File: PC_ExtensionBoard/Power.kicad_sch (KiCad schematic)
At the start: 1 part

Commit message: update schematic: add pattern
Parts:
- added C204, C205, C48, C53, C54, C55: C_100n_0402, antmicro-footprints:C_0402_1005Metric, symbol antmicroCapacitors0402:C_100n_0402
- added C39: C_Pol_68u_16V_Panasonic-TQC-D, antmicro-footprints:C_Pol_EIA-D, symbol antmicroCapacitorspol:C_Pol_68u_16V_Panasonic-TQC-D
- added C40, C58, C59: C_22u_16V_0603, antmicro-footprints:C_0603_1608Metric, symbol antmicroCapacitors0603:C_22u_16V_0603
- added C45, C50, C57, C62, C66, C67, C69, C70: C_1u_0402, antmicro-footprints:C_0402_1005Metric, symbol antmicroCapacitors0402:C_1u_0402
- added C52, C64: C_Pol_100u_10V_KEMET-T520-B, antmicro-footprints:C_Pol_EIA-B, symbol antmicroCapacitorspol:C_Pol_100u_10V_KEMET-T520-B
- added C61: 1uF/16V, A_HDJ_Library:C_0402_1005Metric, symbol Device:C
- added D10, D11, D14, D19: 0402ESDA-05N, A_HDJ_Library:D_0402_1005Metric, symbol Diode:ESD9B5.0ST5G
- added D12: PESD24VS1UL-N, A_HDJ_Library:D_0402_1005Metric, symbol Device:D_Zener
- added D36: BAT54C, antmicro-footprints:SOT-23-3, symbol antmicroDiodesRectifiersSingle:BAT54C
- added D6: TPD2E2U06_SC70, antmicro-footprints:SC70-3, symbol antmicroTVSDiodes:TPD2E2U06_SC70
- added J18: USB_C_Receptacle_USB2.0, A_HDJ_Library:USB_C_Receptacle_G-Switch_GT-USB-7010ASV, symbol Connector:USB_C_Receptacle_USB2.0
- added L2: L_1u8_14A_Coilcraft-XAL6030, antmicro-footprints:L_Coilcraft-XAL6030, symbol antmicroFixedInductors:L_1u8_14A_Coilcraft-XAL6030
- added L3: L_1u8_6.8A_WE-MAPI-4020, antmicro-footprints:L_WE-MAPI-4020, symbol antmicroFixedInductors:L_1u8_6.8A_WE-MAPI-4020
- added Q3: BSS138-7-F, antmicro-footprints:SOT-23-3, symbol antmicroTransistorsFETsMOSFETsSingle:BSS138-7-F
- added Q4: SI7613DN-T1-GE3, antmicro-footprints:Vishay_PowerPAK_1212-8_Single, symbol antmicroTransistorsFETsMOSFETsSingle:SI7613DN-T1-GE3
- added R100, R107, R110: R_15k_0402, antmicro-footprints:R_0402_1005Metric, symbol antmicroResistors0402:R_15k_0402
- added R101, R118: R_100k_0402, antmicro-footprints:R_0402_1005Metric, symbol antmicroResistors0402:R_100k_0402
- added R102, R115, R119: R_0R_0402, antmicro-footprints:R_0402_1005Metric, symbol antmicroResistors0402:R_0R_0402
- added R104, R113: R_0R001_0805, antmicro-footprints:R_0805_2012Metric, symbol antmicroResistorsmisc:R_0R001_0805
- added R105: R_1k_0402, antmicro-footprints:R_0402_1005Metric, symbol antmicroResistors0402:R_1k_0402
- added R108, R116, R86, R92, R96: R_10k_0402, antmicro-footprints:R_0402_1005Metric, symbol antmicroResistors0402:R_10k_0402
- added R109: R_110k_0402, antmicro-footprints:R_0402_1005Metric, symbol antmicroResistors0402:R_110k_0402
- added R117, R87: R_30k_0402, antmicro-footprints:R_0402_1005Metric, symbol antmicroResistors0402:R_30k_0402
- added R37: 10K/1%, A_DFRobot:R_0402, symbol Device:R
- added R40: 1K/1%, A_DFRobot:R_0402, symbol Device:R
- added R47: 56K/1%, A_DFRobot:R_0402, symbol Device:R
- added R91, R99: R_68k_0402, antmicro-footprints:R_0402_1005Metric, symbol antmicroResistors0402:R_68k_0402
- added U19: TPS56C230, antmicro-footprints:QFN-20-1EP_3x3mm_P0.45mm_TPS56xxxx, symbol antmicroDCDCConverters:TPS56C230
- added U20: TPS3840PL30DBVR, antmicro-footprints:SOT-23-5, symbol antmicroPMICPowerSequencers:TPS3840PL30DBVR
- added U21: TPS564247DRLR, antmicro-footprints:SOT-563, symbol antmicroDCDCConverters:TPS564247DRLR
- added U23: TLV73333PDBVT, antmicro-footprints:SOT-23-5, symbol antmicroPMICVoltageRegulatorsLinear:TLV73333PDBVT
- added U49, U50: INA219AIDCNR, antmicro-footprints:SOT-23-8, symbol antmicroPowerMeasurement:INA219AIDCNR
- added U9: CH224K, A_HDJ_Library:ESSOP-10-1EP_3.9x5mm_P1.0mm_EP3.2x2.3, symbol USB PD & DC Input-altium-import:root_0_CH224K
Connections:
- new net: Q3.1 (G), R115.2, R116.1, R117.1
- new net: C61.1, R40.2, U9.1 (VDD)
- new net: C45.2, R91.2, R96.2, U19.17 (V_{CC})
- new net: R107.1, R108.2, U21.5 (EN)
- new net: D36.1, D36.2, R86.1, R87.1, U19.12 (EN)
- new net: C69.2, R119.1, U23.5 (VOUT)
- new net: R102.2, U20.4 (~{MR})
- new net: C53.2, C55.2, U20.5 (CT)
- new net: C48.1, U19.1 (BST)
- new net: R100.2, R99.1, U19.14 (FB)
- new net: R91.1, R92.2, U19.15 (MODE)
- new net: C48.2, L2.1, U19.19 (SW), U19.20 (SW), U19.6 (SW)
- new net: R109.1, R110.2, U21.6 (FB)
- new net: C62.2, C64.1, L3.2, R109.2, R113.1, U50.1 (IN+)
- new net: C50.2, C52.1, L2.2, R104.1, R99.2, U49.1 (IN+)
- new net: Q3.3 (D), Q4.4 (G), R118.1
- new net: R37.2, U9.8 (VBUS)
- new net: R47.1, U9.9 (CFG1)
- new net: L3.1, U21.2 (SW)
- new net +12V: R116.2
- new net +12V_AON: C39.1, C40.2, C58.2, C59.2, R107.2, U19.2 (V_{IN}), U19.3 (V_{IN}), U19.4 (V_{IN}), U19.5 (V_{IN}), U21.1 (V_{IN})
- new net +15V: D12.1 (K), J18.A4 (VBUS), J18.A9 (VBUS), J18.B4 (VBUS), J18.B9 (VBUS), R37.1, R40.1
- new net +3V3: C57.2, R104.2, U49.2 (IN-)
- new net +3V3_AON: C204.2, C205.2, C54.2, R119.2, U20.2 (VDD), U49.4 (V_{S}), U49.7 (A0), U50.4 (V_{S})
- new net +5V: C70.2, Q4.5 (D), R86.2
- new net +5V_AON: C66.2, C67.2, Q4.1 (S), Q4.2 (S), Q4.3 (S), R113.2, R118.2, U23.1 (VIN), U23.3 (EN), U50.2 (IN-)
- new net CC1: D14.2 (A2), J18.A5 (CC1), U9.7 (CC1)
- new net CC2: D19.2 (A2), J18.B5 (CC2), U9.6 (CC2)
- new net GND: C204.1, C205.1, C39.2, C40.1, C45.1, C50.1, C52.2, C53.1, C54.1, C55.1, C57.1, C58.1, C59.1, C61.2, C62.1, C64.2, C66.1, C67.1, C69.1, C70.1, D10.1 (A1), D11.1 (A1), D12.2 (A), D14.1 (A1), D19.1 (A1), D6.3, J18.A1 (GND), J18.A12 (GND), J18.B1 (GND), J18.B12 (GND), J18.S1 (SHIELD), Q3.2 (S), R100.1, R101.1, R105.1, R108.1, R110.1, R117.2, R47.2, R87.2, R92.1, U19.13 (AGND), U19.18 (PGND), U19.21 (PGND), U19.7 (PGND), U19.8 (PGND), U20.3 (GND), U21.3 (GND), U21.4 (AGND), U23.2 (GND), U49.3 (GND), U49.8 (A1), U50.3 (GND), U50.8 (A1), U9.0 (GND)
- new net I2C.SCL: U49.5 (SCL), U50.5 (SCL)
- new net I2C.SDA: U49.6 (SDA), U50.6 (SDA), U50.7 (A0)
- new net PG_{1V0}: R101.2, R102.1
- new net PG_{3V3}: R96.1, U19.9 (PG)
- new net PSON: D36.3
- new net PWRBTN: D6.2
- new net PWR_C_D+: D11.2 (A2), J18.A6 (D+), J18.B6 (D+), U9.4 (DP)
- new net PWR_C_D-: D10.2 (A2), J18.A7 (D-), J18.B7 (D-), U9.5 (DM)
- new net PWR_OK: R105.2, U20.1 (~{RESET})
- new net ~{RESET}: R115.1
- no-connect marks 0 -> 7
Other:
- note added: "+3V3 DC/DC converter"
- note added: "+3V3_AON LDO"
- note added: "+5V DC/DC converter"
- note added: "15V PD Input"
- note added: "1V0 is last in PG chain so then if it's PG is high all rails should be OK"
- note added: "ADDR: 0x41"
- note added: "ADDR: 0x42"
- note added: "CH224K get DC 15V power from USB-PD adapter"
- note added: "PSU rail description: * +12V_{AON} - Input power Always on rails: * +5V_{AON} * +3V3_{AON} Board rails (PSON == 1): * +12V * +5V * +3V3 * +1V8 * +1V0"
- note added: "Sequence: +5V_{AON} +3V3_{AON} *Power button* +12V +5V +3V3 +1V8 +1V0"
- note added: "V_{out} = 3.3 V f_{SW} = 500 kHz I_{L} = 11.0 A ΔI_{L} = 25% I_{Lpeak} = 12.4 A"
- note added: "V_{out} = 5.0 V f_{SW} = 1200 kHz I_{L} = 4.0 A ΔI_{L} = 34% I_{Lpeak} = 4.68 A"
- note added: "~120 ms delay"

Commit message: components placement R1
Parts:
- C61: footprint A_HDJ_Library:C_0402_1005Metric -> PC_Components_1:C_0402_1005Metric; DF_Comment 贴片电容0402-1uF-16V-X5R(0402) -> (none); SCH_Show_Footprint C0402 -> (none)
- D10, D11, D14, D19: footprint A_HDJ_Library:D_0402_1005Metric -> PC_Components_1:C_0402_1005Metric; DF_Comment 5.0V双向静电保护管_0402ESDA-05N -> (none); LCSC (none) -> C316049; SCH_Show_Footprint D0402 -> (none)
- D12: footprint A_HDJ_Library:D_0402_1005Metric -> PC_Components_1:C_0402_1005Metric; Buy_Link https://item.szlcsc.com/393990.html -> (none); DF_Comment 单向静电保护二极管_PESD24VS1UL-N_DFN1006 -> (none); LCSC (none) -> C406227
- R37: footprint A_DFRobot:R_0402 -> PC_Components_1:R_0402_1005Metric; DF_Comment 贴片电阻0402-10K-1% -> (none)
- R40: footprint A_DFRobot:R_0402 -> PC_Components_1:R_0402_1005Metric; DF_Comment 贴片电阻0402-1K-1% -> (none)
- R47: value 56K/1% -> 24K/1%; footprint A_DFRobot:R_0402 -> PC_Components_1:C_0402_1005Metric; DF_Comment 贴片电阻0402-56K-1%(0402) -> (none)
- U9: footprint A_HDJ_Library:ESSOP-10-1EP_3.9x5mm_P1.0mm_EP3.2x2.3 -> PC_ExtensionBoard:ESSOP-10_L4.9-W3.9-P1.0-LS6.0-TL-EP; DF_Comment USB PD等快充协议受电芯片-CH224K-ESSOP10 -> (none); LCSC (none) -> C970725
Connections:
- net +15V is gone; now on net +12V: D12.1 (K), J18.A4 (VBUS), J18.A9 (VBUS), J18.B4 (VBUS), J18.B9 (VBUS), R37.1, R40.1
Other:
- note added: "12V PD Input"
- note added: "CH224K get DC 12V power from USB-PD adapter"
- note removed: "15V PD Input"
- note removed: "1V0 is last in PG chain so then if it's PG is high all rails should be OK"
- note removed: "CH224K get DC 15V power from USB-PD adapter"
- note removed: "PSU rail description: * +12V_{AON} - Input power Always on rails: * +5V_{AON} * +3V3_{AON} Board rails (PSON == 1): * +12V * +5V * +3V3 * +1V8 * +1V0"
- note removed: "Sequence: +5V_{AON} +3V3_{AON} *Power button* +12V +5V +3V3 +1V8 +1V0"
- moved on the sheet: C53, C54, C55, C61, D10, D11, D12, D14, D19, J18, R101, R102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

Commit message: refactor project
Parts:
- C204, C205, C48, C53, C54, C55: symbol antmicroCapacitors0402:C_100n_0402 -> A_PC_ExtensionBoard:C_100n_0402
- C39: symbol antmicroCapacitorspol:C_Pol_68u_16V_Panasonic-TQC-D -> A_PC_ExtensionBoard:C_Pol_68u_16V_Panasonic-TQC-D
- C40, C58, C59: symbol antmicroCapacitors0603:C_22u_16V_0603 -> A_PC_ExtensionBoard:C_22u_16V_0603
- C45, C50, C57, C62, C66, C67, C69, C70: symbol antmicroCapacitors0402:C_1u_0402 -> A_PC_ExtensionBoard:C_1u_0402
- C52, C64: symbol antmicroCapacitorspol:C_Pol_100u_10V_KEMET-T520-B -> A_PC_ExtensionBoard:C_Pol_100u_10V_KEMET-T520-B
- D36: symbol antmicroDiodesRectifiersSingle:BAT54C -> A_PC_ExtensionBoard:BAT54C
- D6: footprint antmicro-footprints:SC70-3 -> PC_Components_1:SC70-3; symbol antmicroTVSDiodes:TPD2E2U06_SC70 -> A_PC_ExtensionBoard:TPD2E2U06_SC70; LCSC (none) -> C1855726
- DC1: symbol ACLAB_Symbol:root_0_DC-044A-20A_ -> A_PC_ExtensionBoard:DC-044A-20A_
- L2: symbol antmicroFixedInductors:L_1u8_14A_Coilcraft-XAL6030 -> A_PC_ExtensionBoard:L_1u8_14A_Coilcraft-XAL6030
- L3: symbol antmicroFixedInductors:L_1u8_6.8A_WE-MAPI-4020 -> A_PC_ExtensionBoard:L_1u8_6.8A_WE-MAPI-4020
- Q3: symbol antmicroTransistorsFETsMOSFETsSingle:BSS138-7-F -> A_PC_ExtensionBoard:BSS138-7-F
- Q4: symbol antmicroTransistorsFETsMOSFETsSingle:SI7613DN-T1-GE3 -> A_PC_ExtensionBoard:SI7613DN-T1-GE3
- R100, R107, R110: symbol antmicroResistors0402:R_15k_0402 -> A_PC_ExtensionBoard:R_15k_0402
- R101, R118: symbol antmicroResistors0402:R_100k_0402 -> A_PC_ExtensionBoard:R_100k_0402
- R102, R115, R119: symbol antmicroResistors0402:R_0R_0402 -> A_PC_ExtensionBoard:R_0R_0402
- R104, R113: symbol antmicroResistorsmisc:R_0R001_0805 -> A_PC_ExtensionBoard:R_0R001_0805
- R105: symbol antmicroResistors0402:R_1k_0402 -> A_PC_ExtensionBoard:R_1k_0402
- R108, R116, R86, R92, R96: symbol antmicroResistors0402:R_10k_0402 -> A_PC_ExtensionBoard:R_10k_0402
- R109: symbol antmicroResistors0402:R_110k_0402 -> A_PC_ExtensionBoard:R_110k_0402
- R117, R87: symbol antmicroResistors0402:R_30k_0402 -> A_PC_ExtensionBoard:R_30k_0402
- R91, R99: symbol antmicroResistors0402:R_68k_0402 -> A_PC_ExtensionBoard:R_68k_0402
- U19: symbol antmicroDCDCConverters:TPS56C230 -> A_PC_ExtensionBoard:TPS56C230
- U20: symbol antmicroPMICPowerSequencers:TPS3840PL30DBVR -> A_PC_ExtensionBoard:TPS3840PL30DBVR
- U21: symbol antmicroDCDCConverters:TPS564247DRLR -> A_PC_ExtensionBoard:TPS564247DRLR
- U23: symbol antmicroPMICVoltageRegulatorsLinear:TLV73333PDBVT -> A_PC_ExtensionBoard:TLV73333PDBVT
- U49, U50: symbol antmicroPowerMeasurement:INA219AIDCNR -> A_PC_ExtensionBoard:INA219AIDCNR
- U9: symbol USB PD & DC Input-altium-import:root_0_CH224K -> A_PC_ExtensionBoard:CH224K
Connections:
- net +3V3 renamed +3.3V

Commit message: re-link symbol
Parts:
- added BT1: Battery CMOS, Connector_JST:JST_PH_B2B-PH-K_1x02_P2.00mm_Vertical, symbol Device:Battery
- added D5: D_Schottky, symbol Device:D_Schottky
- added R15: R_470R_0402, PC_Components_1:R_0402_1005Metric, symbol A_PC_ExtensionBoard:R_470R_0402
- added SW1: K2-1808SN-A4SW, PC_Components_1:KEY-SMD_4P-L4.2-W3.2-P2.20-LS5.1-TL, symbol A_PC_ExtensionBoard:K2-1808SN-A4SW
- C204, C205, C53, C54, C55, C57, C66, C67, C69, C70: footprint antmicro-footprints:C_0402_1005Metric -> PC_Components_1:C_0402_1005Metric
- D36, Q3: footprint antmicro-footprints:SOT-23-3 -> PC_Components_1:SOT-23-3
- L2: footprint antmicro-footprints:L_Coilcraft-XAL6030 -> PC_Components_1:L_Coilcraft-XAL6030
- L3: footprint antmicro-footprints:L_WE-MAPI-4020 -> PC_Components_1:L_WE-MAPI-4020
- Q4: footprint antmicro-footprints:Vishay_PowerPAK_1212-8_Single -> PC_Components_1:Vishay_PowerPAK_1212-8_Single
- R100, R101, R102, R105, R107, R108, R109, R110, R115, R116, R117, R118, R119, R86, R87, R91, R92, R96, R99: footprint antmicro-footprints:R_0402_1005Metric -> PC_Components_1:R_0402_1005Metric
- R104, R113: footprint antmicro-footprints:R_0805_2012Metric -> PC_Components_1:R_0402_1005Metric
- U19: footprint antmicro-footprints:QFN-20-1EP_3x3mm_P0.45mm_TPS56xxxx -> PC_Components_1:QFN-20-1EP_3x3mm_P0.45mm_TPS56xxxx
- U20, U23: footprint antmicro-footprints:SOT-23-5 -> PC_Components_1:SOT-23-5
- U21: footprint antmicro-footprints:SOT-563 -> PC_Components_1:SOT-563
- U49, U50: footprint antmicro-footprints:SOT-23-8 -> PC_Components_1:SOT-23-8
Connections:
- net GND: now also BT1.2 (-), SW1.1, SW1.2
- net PWRBTN: now also SW1.3, SW1.4
- new net: BT1.1 (+), R15.1
- new net: D5.2 (A), R15.2
- new net VCC_RTC: D5.1 (K)

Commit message: update LCSC for HDMI
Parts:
- removed J18: USB_C_Receptacle_USB2.0, A_HDJ_Library:USB_C_Receptacle_G-Switch_GT-USB-7010ASV, symbol Connector:USB_C_Receptacle_USB2.0
- added USBC1: J18, PC_Components_1:USB-C_SMD-TYPE-C-31-M-12_1, symbol A_PC_ExtensionBoard:root_0_TYPE-C-31-M-12__1
- C204, C205, C48, C53, C54, C55: LCSC (none) -> C85960
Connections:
- net +12V: now also USBC1.A4B9 (VBUS), USBC1.B4A9 (VBUS)
- net CC1: now also USBC1.A5 (CC1)
- net CC2: now also USBC1.B5 (CC2)
- net GND: now also USBC1.1 (EH), USBC1.2 (EH), USBC1.3 (EH), USBC1.4 (EH), USBC1.A1B12 (GND), USBC1.B1A12 (GND)
- net PWR_C_D+: now also USBC1.A6 (DP1), USBC1.B6 (DP2)
- net PWR_C_D-: now also USBC1.A7 (DN1), USBC1.B7 (DN2)
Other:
- moved on the sheet: D6, DC1, SW1

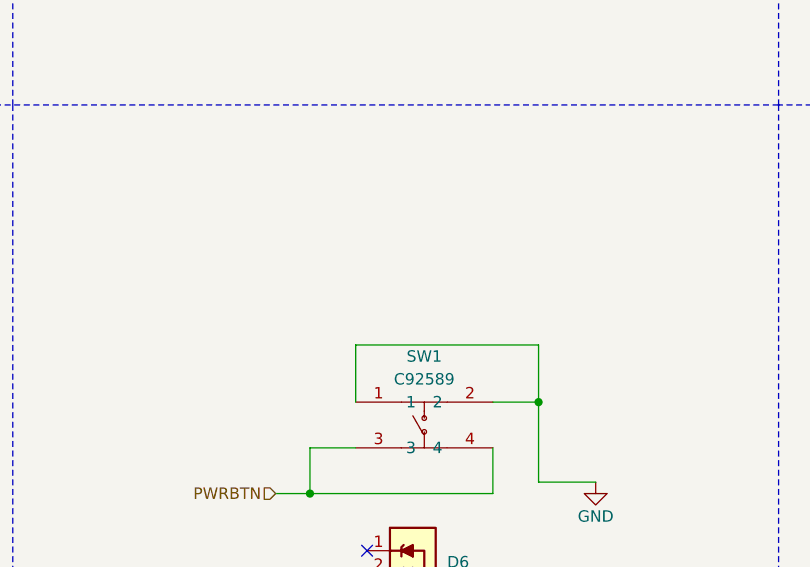
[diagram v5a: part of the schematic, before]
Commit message: update LCSC
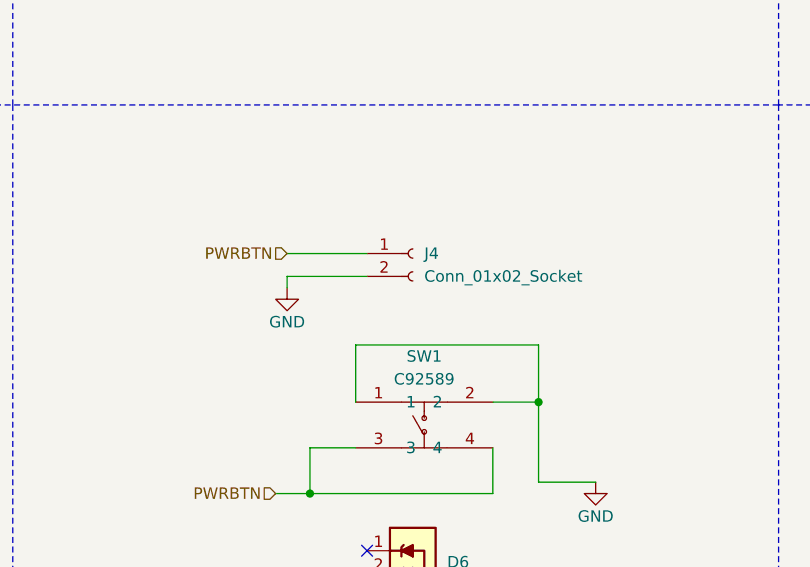
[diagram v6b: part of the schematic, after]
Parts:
- added J4: Conn_01x02_Socket, PC_Components_1:CONN-SMD_2P-P2.00_BX-PH2.0-2PWT, symbol Connector:Conn_01x02_Socket
- D5: footprint (none) -> PC_Components_1:D_SOD-323; LCSC (none) -> C168799
- R15: LCSC (none) -> C2077077
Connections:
- net GND: now also J4.2 (Pin_2)
- net PWRBTN: now also J4.1 (Pin_1)

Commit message: schematic changes
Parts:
- added D8: TPD2E2U06_SC70, PC_Components_1:SC70-3, symbol A_PC_ExtensionBoard:TPD2E2U06_SC70
- added J5: Conn_01x02_Socket, PC_Components_1:CONN-SMD_2P-P2.00_BX-PH2.0-2PWT, symbol Connector:Conn_01x02_Socket
- added SW2: K2-1808SN-A4SW, PC_Components_1:KEY-SMD_4P-L4.2-W3.2-P2.20-LS5.1-TL, symbol A_PC_ExtensionBoard:K2-1808SN-A4SW
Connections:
- net GND: now also D8.3, J5.2 (Pin_2), SW2.1, SW2.2
- new net RESETBTN: D8.2, J5.1 (Pin_1), SW2.3, SW2.4
- no-connect marks 7 -> 8
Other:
- moved on the sheet: C66, C69, R119, U23

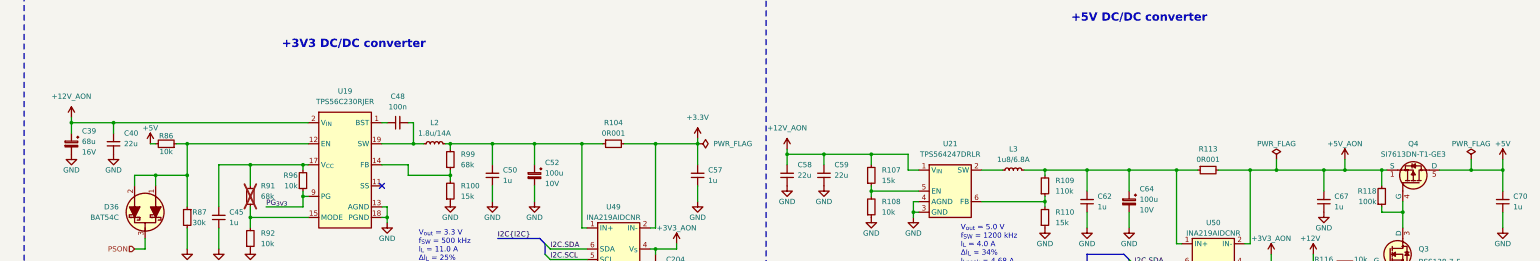
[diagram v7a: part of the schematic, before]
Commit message: update schematic
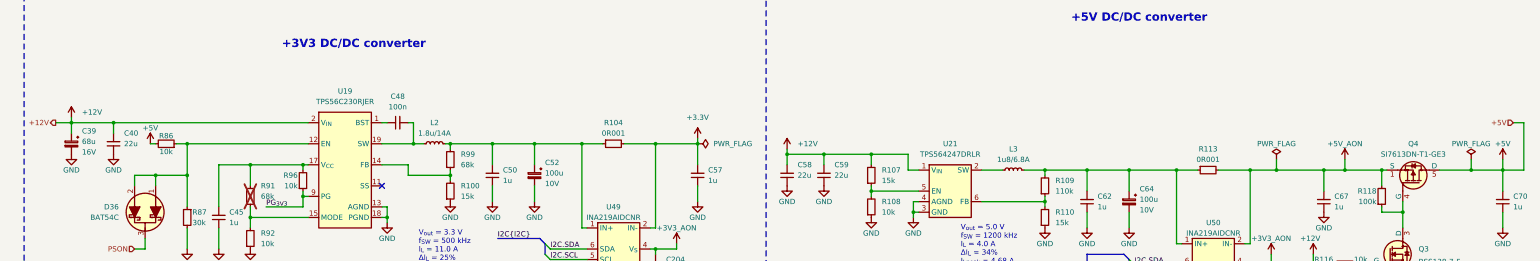
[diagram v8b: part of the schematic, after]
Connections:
- net +12V_AON is gone; now on net +12V: C39.1, C40.2, C58.2, C59.2, R107.2, U19.2 (V_{IN}), U19.3 (V_{IN}), U19.4 (V_{IN}), U19.5 (V_{IN}), U21.1 (V_{IN})
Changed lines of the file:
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@@
 	(wire
 		(pts
+			(xy 226.06 50.8) (xy 229.87 50.8)
+		)
+		(stroke
+			(width 0)
+			(type default)
+		)
+	)
+	(wire
+		(pts
 			(xy 346.71 92.71) (xy 351.79 92.71)
 		)
@@
 	(wire
 		(pts
+			(xy 580.39 62.23) (xy 575.31 62.23)
+		)
+		(stroke
+			(width 0)
+			(type default)
+		)
+	)
+	(wire
+		(pts
 			(xy 467.36 227.33) (xy 467.36 229.87)
 		)
@@
 	(wire
 		(pts
+			(xy 577.85 50.8) (xy 580.39 50.8)
+		)
+		(stroke
+			(width 0)
+			(type default)
+		)
+	)
+	(wire
+		(pts
 			(xy 537.21 62.23) (xy 546.1 62.23)
 		)
@@
 	(wire
 		(pts
+			(xy 580.39 50.8) (xy 580.39 62.23)
+		)
+		(stroke
+			(width 0)
+			(type default)
+		)
+	)
+	(wire
+		(pts
 			(xy 311.15 60.96) (xy 311.15 63.5)
 		)
@@
 		)
 	)
+	(hierarchical_label "+5V"
+		(shape input)
+		(at 577.85 50.8 180)
+		(effects
+			(font
+				(size 1.27 1.27)
+			)
+			(justify right)
+		)
+	)
+	(hierarchical_label "+12V"
+		(shape output)
+		(at 226.06 50.8 180)
+		(effects
+			(font
+				(size 1.27 1.27)
+			)
+			(justify right)
+		)
+	)
 	(hierarchical_label "I2C{I2C}"
 		(shape input)
@@
 			)
 		)
-		(property "Value" "+12V_AON"
-			(at 229.87 44.45 0)
+		(property "Value" "+12V"
+			(at 232.41 48.2599 0)
 			(show_name no)
 			(do_not_autoplace no)
@@
 					(size 1.27 1.27)
 				)
+				(justify left)
 			)
 		)
@@
 			)
 		)
-		(property "Value" "+12V_AON"
-			(at 402.59 52.07 0)
+		(property "Value" "+12V"
+			(at 405.13 55.8799 0)
 			(show_name no)
 			(do_not_autoplace no)
@@
 					(size 1.27 1.27)
 				)
+				(justify left)
 			)
 		)
